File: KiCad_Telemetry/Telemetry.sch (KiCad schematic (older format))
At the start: 37 parts, among them IC1 TCAN1044VDRQ1, J2 Conn_01x03, J3 PinHeader_01x02, J4 PinHeader_01x02, J5 PinHeader_01x02, J7 DB9_Female, J8 USB_A Connector, U1 NRF24L01_Breakout, U2 STM32F042C4T6, U3 TLV70033_SOT23-5, U4 MCP2518FDT, Y1 Crystal_GND24

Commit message: Revised layout, Created GERBER and Drill Files. Finished BOM
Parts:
- removed J5: PinHeader_01x02, Connector_PinHeader_2.54mm:PinHeader_1x02_P2.54mm_Vertical, symbol Connector_Generic:Conn_01x02
- H1, H2, H3, H4: footprint MountingHole:MountingHole_3.5mm -> MountingHole:MountingHole_3.5mm_Pad_Via; symbol Mechanical:MountingHole -> Mechanical:MountingHole_Pad
- J8: value USB_A Connector -> USB Micro Connector; footprint Connector_USB:USB_A_Stewart_SS-52100-001_Horizontal -> Connector_USB:USB_Micro-B_Molex-105017-0001; symbol Connector:USB_A -> Connector:USB_B_Micro; MouserNO 530-SS-52100-001 -> 538-105017-0001; UnitPrice 0.387 -> 0,792
- U4: Description (none) -> The STM32 cannot handle CAN-FD, this chip is an SPI to CAN-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; MouserNO (none) -> 579-MCP2518FDT-H/SL; UnitPrice (none) -> 1,44
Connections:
- net GND: now also H1.1, H2.1, H3.1, H4.1; no longer J8.4 (GND)
- net USB_DM renamed USB_D-
- net USB_DP renamed USB_D+
- no-connect marks 25 -> 27
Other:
- note removed: "DTU ROAST Telemetry Module"
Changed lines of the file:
@@
 External Clock
 Text GLabel 2600 6900 2    50   Input ~ 0
-USB_DP
+USB_D+
 Text GLabel 2600 6800 2    50   Input ~ 0
-USB_DM
+USB_D-
 Text GLabel 1200 7100 0    50   Input ~ 0
 SPI2_SCK
@@
 $EndComp
 $Comp
-L Mechanical:MountingHole H1
+L Mechanical:MountingHole_Pad H1
 U 1 1 5EACA05D
 P 3400 700
 F 0 "H1" H 3500 746 50  0000 L CNN
 F 1 "MountingHole" H 3500 655 50  0000 L CNN
-F 2 "MountingHole:MountingHole_3.5mm" H 3400 700 50  0001 C CNN
+F 2 "MountingHole:MountingHole_3.5mm_Pad_Via" H 3400 700 50  0001 C CNN
 F 3 "~" H 3400 700 50  0001 C CNN
 	1    3400 700
@@
 $EndComp
 $Comp
-L Mechanical:MountingHole H2
+L Mechanical:MountingHole_Pad H2
 U 1 1 5EACC8D0
-P 3400 900
-F 0 "H2" H 3500 946 50  0000 L CNN
-F 1 "MountingHole" H 3500 855 50  0000 L CNN
-F 2 "MountingHole:MountingHole_3.5mm" H 3400 900 50  0001 C CNN
-F 3 "~" H 3400 900 50  0001 C CNN
-	1    3400 900
-	1    0    0    -1
-$EndComp
-$Comp
-L Mechanical:MountingHole H3
-U 1 1 5EACCCEE
-P 3400 1100
-F 0 "H3" H 3500 1146 50  0000 L CNN
-F 1 "MountingHole" H 3500 1055 50  0000 L CNN
-F 2 "MountingHole:MountingHole_3.5mm" H 3400 1100 50  0001 C CNN
-F 3 "~" H 3400 1100 50  0001 C CNN
-	1    3400 1100
-	1    0    0    -1
-$EndComp
-$Comp
-L Mechanical:MountingHole H4
+P 4100 700
+F 0 "H2" H 4200 746 50  0000 L CNN
+F 1 "MountingHole" H 4200 655 50  0000 L CNN
+F 2 "MountingHole:MountingHole_3.5mm_Pad_Via" H 4100 700 50  0001 C CNN
+F 3 "~" H 4100 700 50  0001 C CNN
+	1    4100 700
+	1    0    0    -1
+$EndComp
+$Comp
+L Mechanical:MountingHole_Pad H4
 U 1 1 5EACCF43
-P 3400 1300
-F 0 "H4" H 3500 1346 50  0000 L CNN
-F 1 "MountingHole" H 3500 1255 50  0000 L CNN
-F 2 "MountingHole:MountingHole_3.5mm" H 3400 1300 50  0001 C CNN
-F 3 "~" H 3400 1300 50  0001 C CNN
-	1    3400 1300
+P 3400 1200
+F 0 "H4" H 3500 1246 50  0000 L CNN
+F 1 "MountingHole" H 3500 1155 50  0000 L CNN
+F 2 "MountingHole:MountingHole_3.5mm_Pad_Via" H 3400 1200 50  0001 C CNN
+F 3 "~" H 3400 1200 50  0001 C CNN
+	1    3400 1200
 	1    0    0    -1
 $EndComp
@@
 Wire Wire Line
 	1700 1100 1700 1150
-$Comp
-L Connector_Generic:Conn_01x02 J5
-U 1 1 5EBC0206
-P 9050 6350
-F 0 "J5" H 9130 6342 50  0000 L CNN
-F 1 "PinHeader_01x02" H 8700 6100 50  0000 L CNN
-F 2 "Connector_PinHeader_2.54mm:PinHeader_1x02_P2.54mm_Vertical" H 9050 6350 50  0001 C CNN
-F 3 "https://www.mouser.dk/datasheet/2/181/M20-973-1273432.pdf" H 9050 6350 50  0001 C CNN
-F 4 "855-M20-9730245 " H 9050 6350 50  0001 C CNN "MouserNO"
-F 5 "0,144" H 9050 6350 50  0001 C CNN "UnitPrice"
-F 6 "Supply Pinheaders for debugging" H 9050 6350 50  0001 C CNN "Description"
-	1    9050 6350
-	1    0    0    1
-$EndComp
-Text GLabel 8850 6350 0    50   Input ~ 0
-CAN-
-Text GLabel 8850 6250 0    50   Input ~ 0
-CAN+
 Text GLabel 10050 6050 0    50   Input ~ 0
 CAN+
-Text GLabel 10050 5950 0    50   Input ~ 0
-CAN-
-$Comp
-L power:GND #PWR030
-U 1 1 5EC183F7
-P 9700 5850
-F 0 "#PWR030" H 9700 5600 50  0001 C CNN
-F 1 "GND" H 9705 5677 50  0000 C CNN
-F 2 "" H 9700 5850 50  0001 C CNN
-F 3 "" H 9700 5850 50  0001 C CNN
-	1    9700 5850
-	-1   0    0    -1
-$EndComp
 Wire Wire Line
 	10050 6050 10200 6050
@@
 	10050 5950 10200 5950
 Wire Wire Line
-	9700 5850 9950 5850
-Wire Wire Line
 	10200 5550 9950 5550
-Wire Wire Line
-	9700 5550 9700 5500
-$Comp
-L power:VCC #PWR029
-U 1 1 5ECA4ED3
-P 9700 5500
-F 0 "#PWR029" H 9700 5350 50  0001 C CNN
-F 1 "VCC" H 9717 5673 50  0000 C CNN
-F 2 "" H 9700 5500 50  0001 C CNN
-F 3 "" H 9700 5500 50  0001 C CNN
-	1    9700 5500
-	1    0    0    -1
-$EndComp
 $Comp
 L B3F-4000:B3F-4000 S1
@@
 $EndComp
 Connection ~ 9950 5550
-Wire Wire Line
-	9950 5550 9700 5550
 $Comp
 L power:PWR_FLAG #FLG0102
@@
 Text Notes 2300 3900 0    50   ~ 0
 According to Datasheet
-Text Notes 7350 7500 0    50   ~ 0
-DTU ROAST Telemetry Module
 $Comp
 L power:VCC #PWR033
@@
 	10450 4250 10200 4250
 $Comp
-L Connector:USB_A J8
+L Connector:USB_B_Micro J8
 U 1 1 5E7F3D0D
 P 10750 4450
 F 0 "J8" H 10807 4917 50  0000 C CNN
-F 1 "USB_A Connector" H 10807 4826 50  0000 C CNN
-F 2 "Connector_USB:USB_A_Stewart_SS-52100-001_Horizontal" H 10900 4400 50  0001 C CNN
-F 3 "https://www.mouser.dk/datasheet/2/643/ds-stw-usb-2.0-and-3.0-connectors-1660615.pdf" H 10900 4400 50  0001 C CNN
-F 4 "530-SS-52100-001" H 10750 4450 50  0001 C CNN "MouserNO"
-F 5 "0.387" H 10750 4450 50  0001 C CNN "UnitPrice"
+F 1 "USB Micro Connector" H 10807 4826 50  0000 C CNN
+F 2 "Connector_USB:USB_Micro-B_Molex-105017-0001" H 10900 4400 50  0001 C CNN
+F 3 "https://www.mouser.dk/datasheet/2/276/1/1050170001_IO_CONNECTORS-230168.pdf" H 10900 4400 50  0001 C CNN
+F 4 "538-105017-0001 " H 10750 4450 50  0001 C CNN "MouserNO"
+F 5 "0,792" H 10750 4450 50  0001 C CNN "UnitPrice"
 F 6 "USB Connection for 5V Supply and PC Communication" H 10750 4450 50  0001 C CNN "Description"
 	1    10750 4450
 	-1   0    0    -1
 $EndComp
-$Comp
-L power:GND #PWR038
-U 1 1 5E82E57A
-P 10800 5000
-F 0 "#PWR038" H 10800 4750 50  0001 C CNN
-F 1 "GND" H 10805 4827 50  0000 C CNN
-F 2 "" H 10800 5000 50  0001 C CNN
-F 3 "" H 10800 5000 50  0001 C CNN
-	1    10800 5000
-	-1   0    0    -1
-$EndComp
-Wire Wire Line
-	10800 5000 10800 4900
-Wire Wire Line
-	10800 4900 10850 4900
-Wire Wire Line
-	10850 4900 10850 4850
-Connection ~ 10800 4900
-Wire Wire Line
-	10800 4900 10750 4900
 Text GLabel 10300 4550 0    50   Input ~ 0
-USB_DM
+USB_D-
 Text GLabel 10300 4450 0    50   Input ~ 0
-USB_DP
+USB_D+
 Wire Wire Line
 	10300 4450 10450 4450
@@
 F 2 "Package_SO:SOIC-14_3.9x8.7mm_P1.27mm" H 5000 1650 50  0001 C CNN
 F 3 "https://ww1.microchip.com/downloads/en/DeviceDoc/20005688A.pdf" H 5000 2900 50  0001 C CNN
+F 4 "579-MCP2518FDT-H/SL " H 5000 2650 50  0001 C CNN "MouserNO"
+F 5 "1,44" H 5000 2650 50  0001 C CNN "UnitPrice"
+F 6 "The STM32 cannot handle CAN-FD, this chip is an SPI to CAN-FD Controller to migigate this issue" H 5000 2650 50  0001 C CNN "Description"
 	1    5000 2650
 	1    0    0    -1
@@
 Text Notes 7050 6900 0    50   ~ 0
 This module is capable of:\n - Reading and writing to a 5V CAN-FD (or CAN 2.0B) bus.\n - Reading and writing to an external computer via USB\n - Transmitting and receiving data wirelessly through an NRF24 up to 1000 metres away
+Wire Wire Line
+	9650 5550 9650 5500
+Wire Wire Line
+	9950 5550 9650 5550
+$Comp
+L power:VCC #PWR029
+U 1 1 5ECA4ED3
+P 9650 5500
+F 0 "#PWR029" H 9650 5350 50  0001 C CNN
+F 1 "VCC" H 9667 5673 50  0000 C CNN
+F 2 "" H 9650 5500 50  0001 C CNN
+F 3 "" H 9650 5500 50  0001 C CNN
+	1    9650 5500
+	1    0    0    -1
+$EndComp
+Wire Wire Line
+	9650 5850 9950 5850
+$Comp
+L power:GND #PWR030
+U 1 1 5EC183F7
+P 9650 5850
+F 0 "#PWR030" H 9650 5600 50  0001 C CNN
+F 1 "GND" H 9655 5677 50  0000 C CNN
+F 2 "" H 9650 5850 50  0001 C CNN
+F 3 "" H 9650 5850 50  0001 C CNN
+	1    9650 5850
+	-1   0    0    -1
+$EndComp
+Text GLabel 10050 5950 0    50   Input ~ 0
+CAN-
+$Comp
+L Mechanical:MountingHole_Pad H3
+U 1 1 5EACCCEE
+P 4100 1200
+F 0 "H3" H 4200 1246 50  0000 L CNN
+F 1 "MountingHole" H 4200 1155 50  0000 L CNN
+F 2 "MountingHole:MountingHole_3.5mm_Pad_Via" H 4100 1200 50  0001 C CNN
+F 3 "~" H 4100 1200 50  0001 C CNN
+	1    4100 1200
+	1    0    0    -1
+$EndComp
+$Comp
+L power:GND #PWR038
+U 1 1 5E82E57A
+P 10750 4900
+F 0 "#PWR038" H 10750 4650 50  0001 C CNN
+F 1 "GND" H 10755 4727 50  0000 C CNN
+F 2 "" H 10750 4900 50  0001 C CNN
+F 3 "" H 10750 4900 50  0001 C CNN
+	1    10750 4900
+	-1   0    0    -1
+$EndComp
+$Comp
+L power:GND #PWR0107
+U 1 1 5EC66E9E
+P 3400 1300
+F 0 "#PWR0107" H 3400 1050 50  0001 C CNN
+F 1 "GND" H 3405 1127 50  0000 C CNN
+F 2 "" H 3400 1300 50  0001 C CNN
+F 3 "" H 3400 1300 50  0001 C CNN
+	1    3400 1300
+	1    0    0    -1
+$EndComp
+$Comp
+L power:GND #PWR0108
+U 1 1 5EC6780D
+P 4100 1300
+F 0 "#PWR0108" H 4100 1050 50  0001 C CNN
+F 1 "GND" H 4105 1127 50  0000 C CNN
+F 2 "" H 4100 1300 50  0001 C CNN
+F 3 "" H 4100 1300 50  0001 C CNN
+	1    4100 1300
+	1    0    0    -1
+$EndComp
+$Comp
+L power:GND #PWR0109
+U 1 1 5EC679AE
+P 4100 800
+F 0 "#PWR0109" H 4100 550 50  0001 C CNN
+F 1 "GND" H 4105 627 50  0000 C CNN
+F 2 "" H 4100 800 50  0001 C CNN
+F 3 "" H 4100 800 50  0001 C CNN
+	1    4100 800
+	1    0    0    -1
+$EndComp
+$Comp
+L power:GND #PWR0110
+U 1 1 5EC67B95
+P 3400 800
+F 0 "#PWR0110" H 3400 550 50  0001 C CNN
+F 1 "GND" H 3405 627 50  0000 C CNN
+F 2 "" H 3400 800 50  0001 C CNN
+F 3 "" H 3400 800 50  0001 C CNN
+	1    3400 800
+	1    0    0    -1
+$EndComp
+NoConn ~ 10850 4850
+NoConn ~ 10450 4650
 $EndSCHEMATC

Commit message: Minor edits; Generated gerber files
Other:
- note added: "DTU ROAST Telemetry Module"
- note added: "Small differential trace"
- note added: "USB 2.0 Fullspeed, No impedance matching necessary"
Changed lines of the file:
@@
 Text Notes 9850 5200 0    50   ~ 0
 CAN Bus Connector
-Text Notes 10050 3800 0    50   ~ 0
+Text Notes 9350 3800 0    50   ~ 0
 USB Connector
-Text Notes 9750 3900 0    50   ~ 0
+Text Notes 9050 3900 0    50   ~ 0
 Pull resistors built into STM32
 Text Notes 8650 4600 0    50   ~ 0
@@
 Wire Notes Line
 	11150 6450 7050 6450
-Text Notes 8750 3800 0    50   ~ 0
+Text Notes 7700 3800 0    50   ~ 0
 Connectors
 Wire Notes Line
@@
 NoConn ~ 10850 4850
 NoConn ~ 10450 4650
+Text Notes 9200 4100 0    50   ~ 0
+Small differential trace
+Text Notes 8450 4000 0    50   ~ 0
+USB 2.0 Fullspeed, No impedance matching necessary
+Text Notes 7400 7500 0    50   ~ 0
+DTU ROAST Telemetry Module
 $EndSCHEMATC

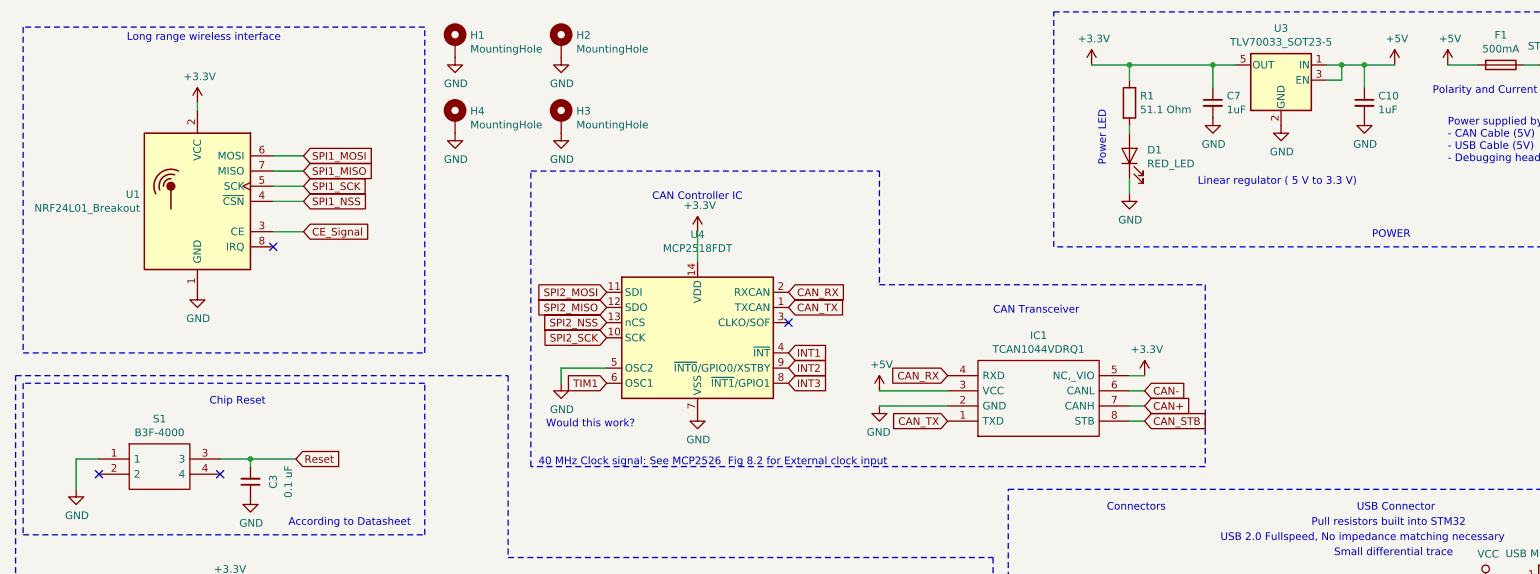
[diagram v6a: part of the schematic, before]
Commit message: Added additional decoupling capacitors; Added Finished design sent to production
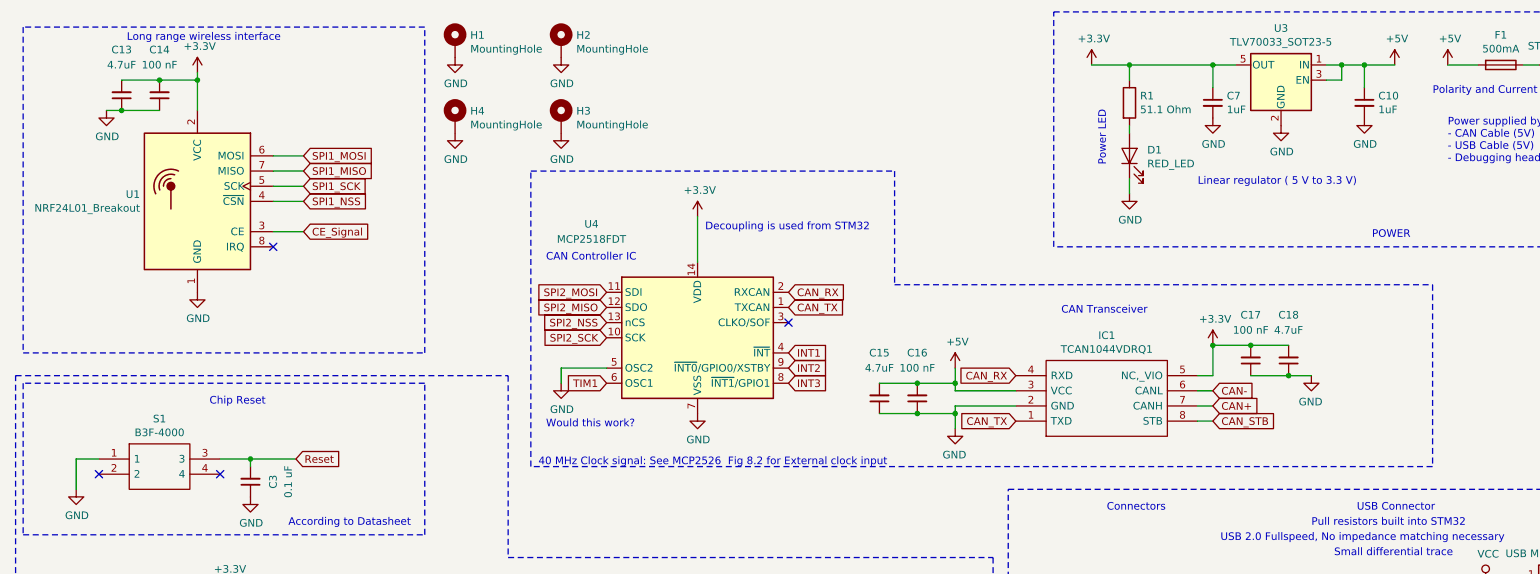
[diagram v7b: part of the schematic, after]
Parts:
- added C13, C15, C18: 4.7uF, Capacitor_SMD:C_0402_1005Metric, symbol Device:C_Small
- added C14, C16, C17: 100 nF, Capacitor_SMD:C_0402_1005Metric, symbol Device:C_Small
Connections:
- net +3V3: now also C13.2, C14.2, C17.2, C18.2
- net +5V: now also C15.2, C16.2
- net GND: now also C13.1, C14.1, C15.1, C16.1, C17.1, C18.1
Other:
- note added: "Decoupling is used from STM32"
- moved on the sheet: IC1
